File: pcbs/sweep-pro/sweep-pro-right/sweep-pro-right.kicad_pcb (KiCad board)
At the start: 2 copper layers, 115 x 86.7 mm, 50 parts, among them J1 Conn_01x04_Female, J2 Conn_01x04_Female, J3 expantion1, SW1 SW_PUSH-kbd, SW10 SW_PUSH-kbd, SW11 SW_PUSH-kbd, SW12 SW_PUSH-kbd, SW13 SW_PUSH-kbd, SW14 SW_PUSH-kbd, SW15 SW_PUSH-kbd, SW16 SW_PUSH-kbd, SW17 SW_PUSH-kbd, SW2 SW_PUSH-kbd, SW3 SW_PUSH-kbd, SW4 SW_PUSH-kbd, SW5 SW_PUSH-kbd, SW6 SW_PUSH-kbd, SW7 SW_PUSH-kbd, SW8 SW_PUSH-kbd, SW9 SW_PUSH-kbd, U1 ProMicro-kbd

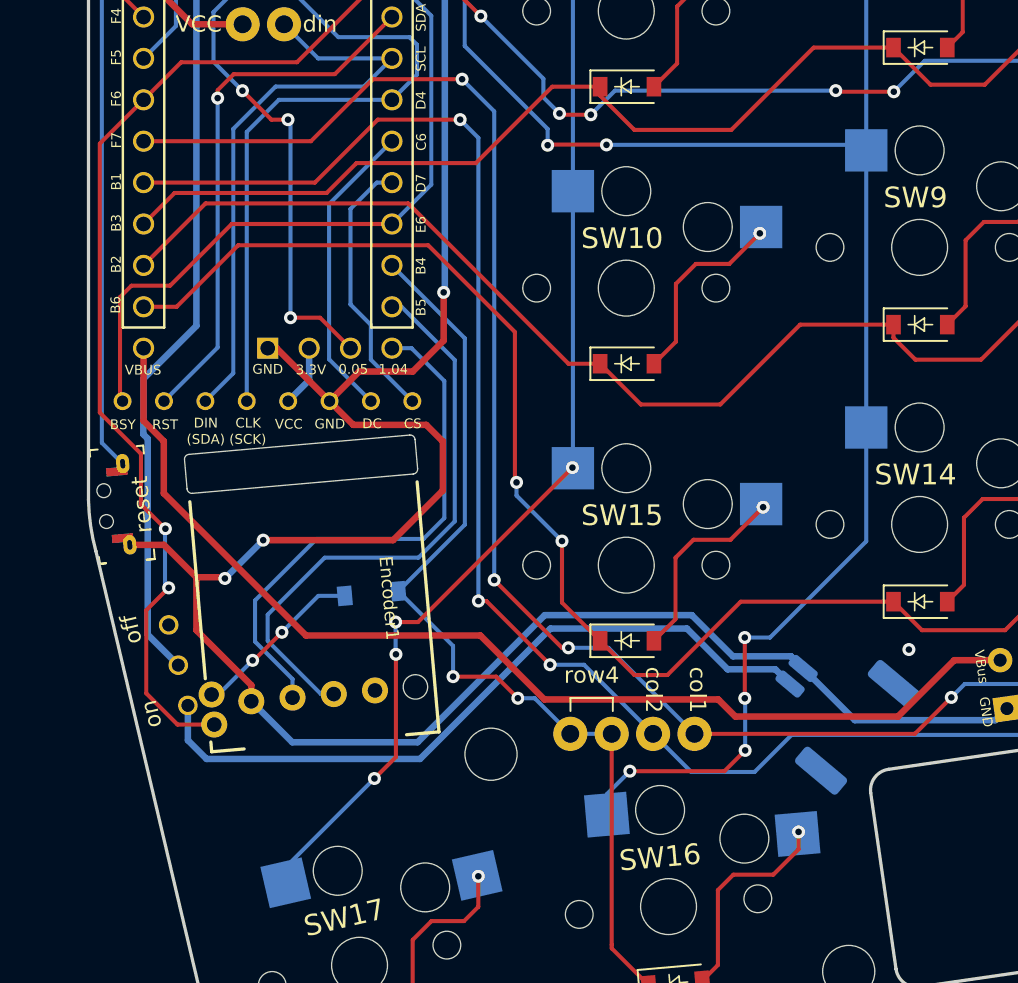
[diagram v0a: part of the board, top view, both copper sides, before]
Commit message: [sweep-pro] correct the position of the encoder in right split
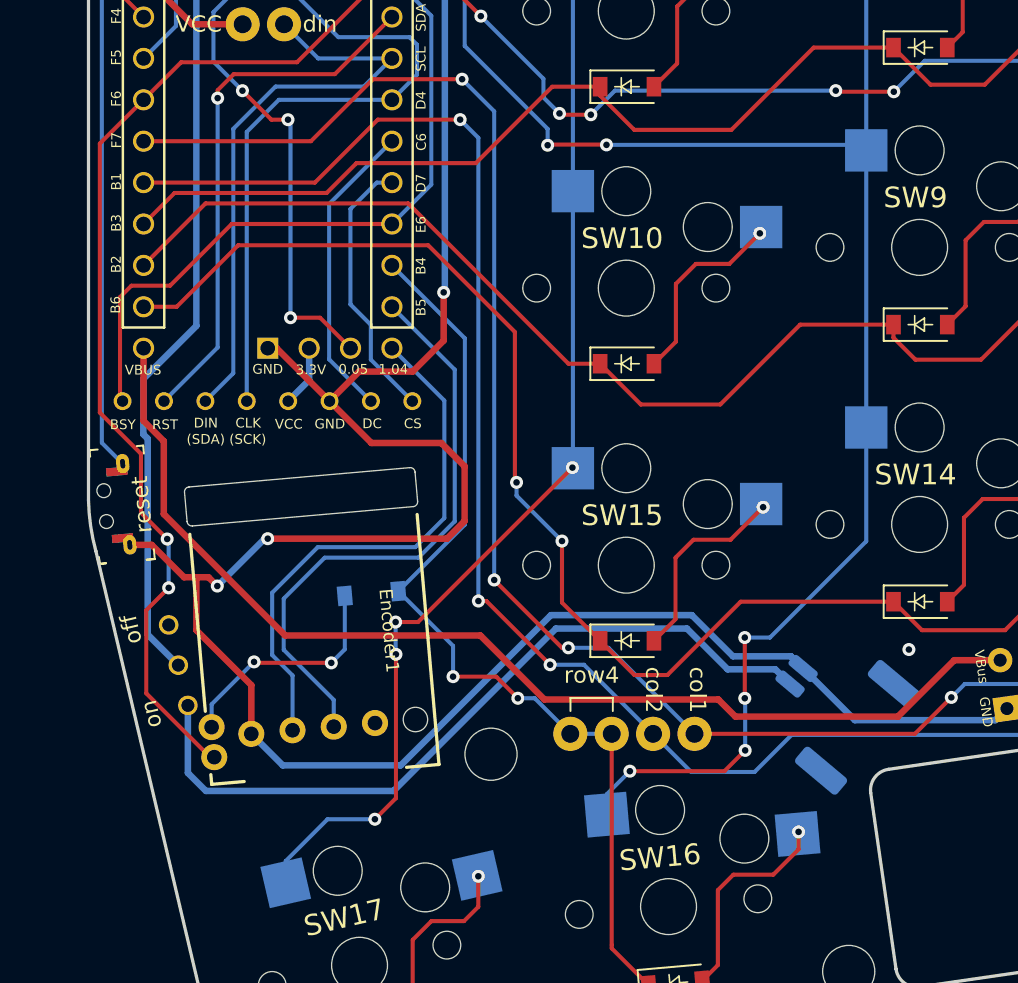
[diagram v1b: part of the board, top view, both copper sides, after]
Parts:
- moved Encoder1 2.00 mm to (96.0, 96.8)
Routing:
- net GND: track 156.7 -> 162.3 mm
- net Net-(D18-Pad2): track 10.7 -> 14.3 mm
- net VBat: track 44.3 -> 47.1 mm
- net col5: track 110.8 -> 112.5 mm
- net col3: track 148.9 -> 149.7 mm
- net VBus: track 67.8 -> 68.6 mm
